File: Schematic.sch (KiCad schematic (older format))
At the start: 22 parts, among them J1 S2B-PH-K-S_LF__SN_, J2 Conn_01x04_Female, J3 Conn_02x05_Odd_Even, J4 Conn_01x05_Female, Q1 BSS138, Q2 BSS138, Q3 BSS138, U1 MDBT42Q, U2 AP7333-33SAG

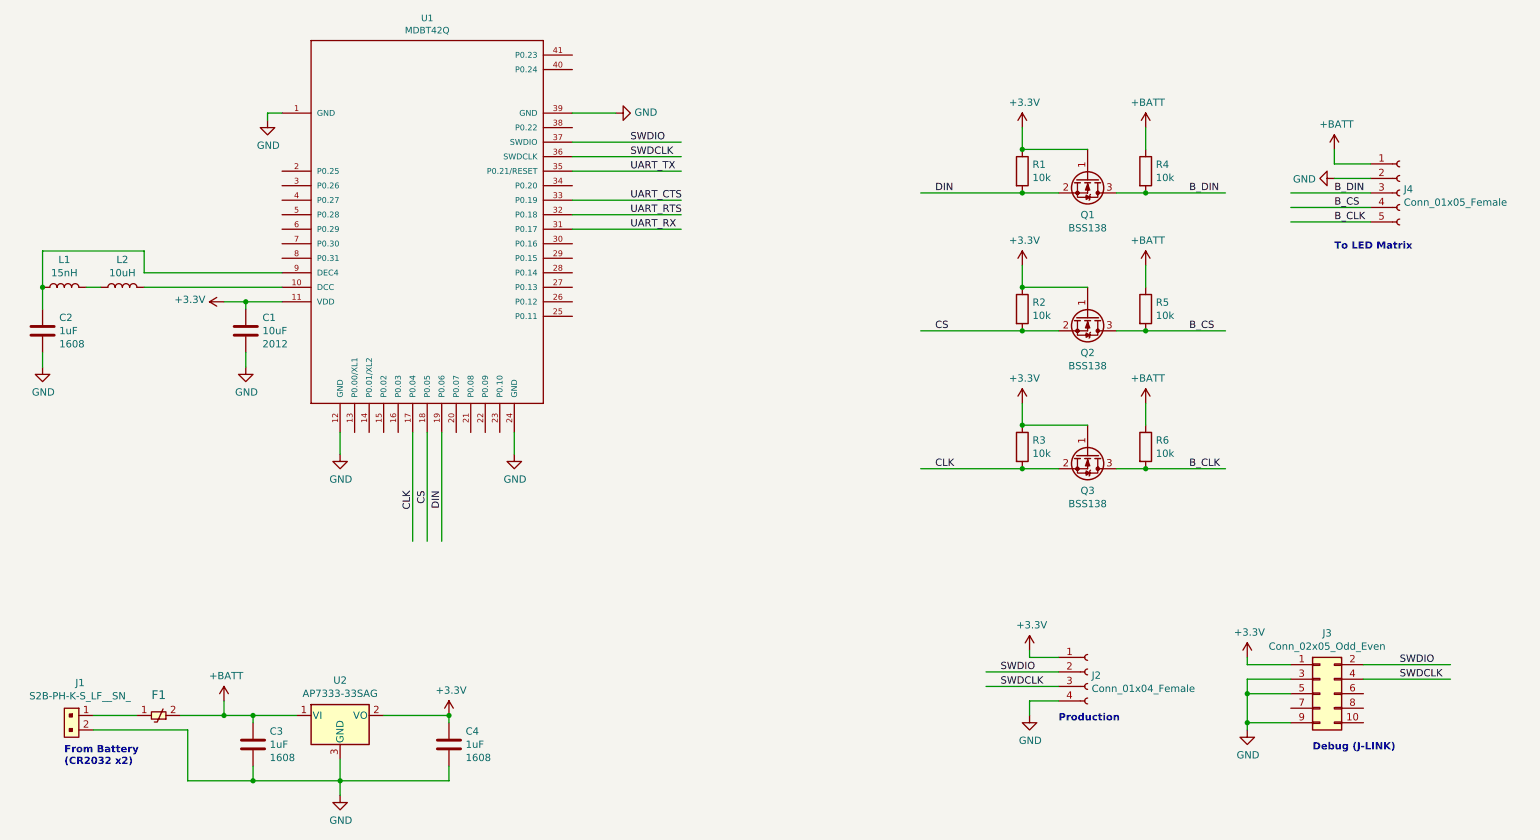
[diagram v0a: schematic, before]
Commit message: TP等を追加
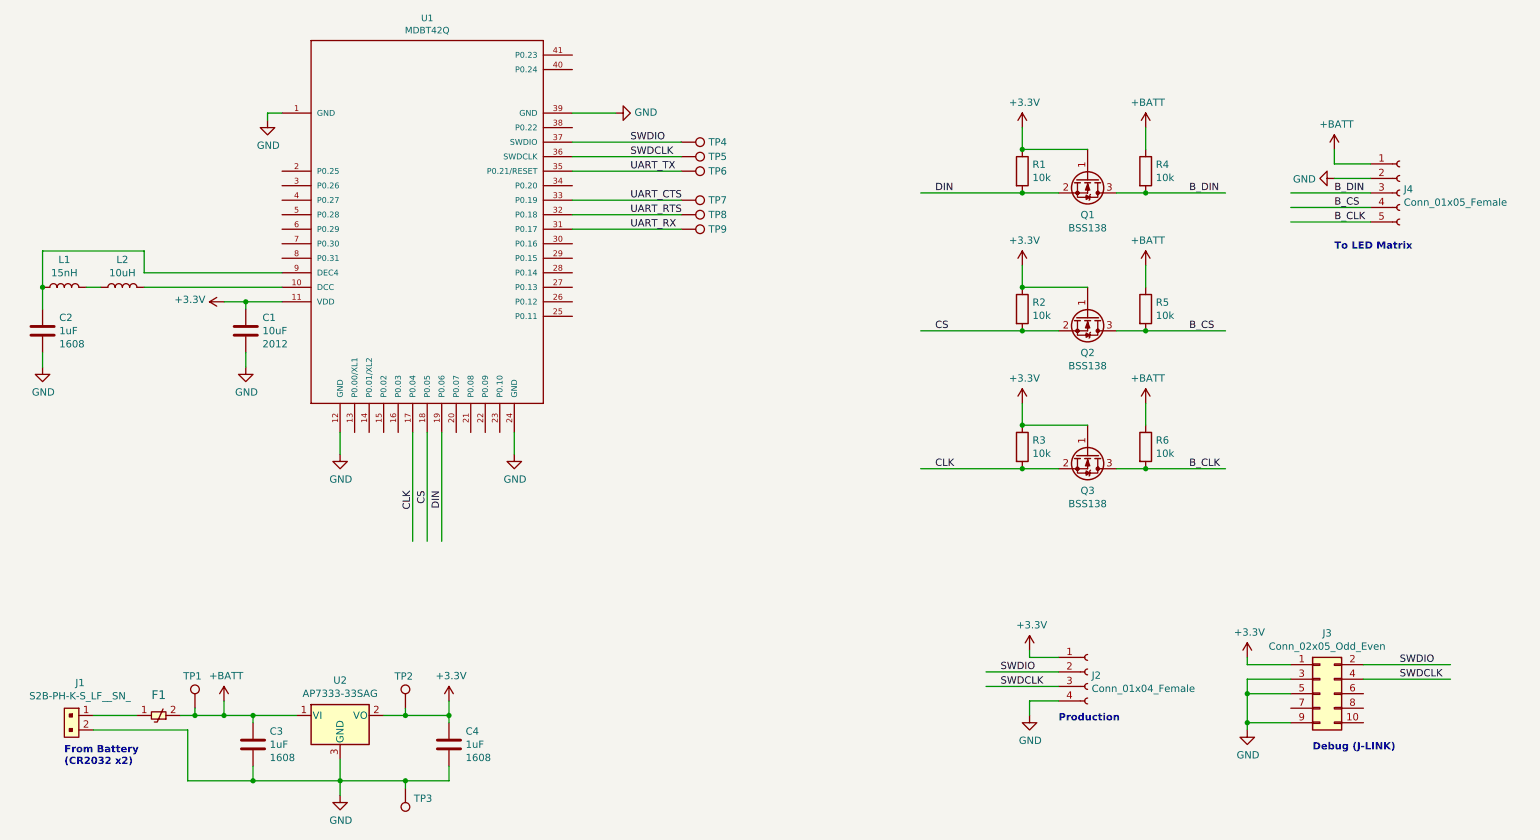
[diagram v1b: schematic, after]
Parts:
- added TP1, TP2, TP3, TP4, TP5, TP6, TP7, TP8, TP9: TestPoint, TestPoint:TestPoint_Pad_D1.5mm, symbol Connector:TestPoint
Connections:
- wire segments 86 -> 93
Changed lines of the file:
@@
 	4250 4200 4250 4050
-Wire Wire Line
-	5400 2050 4650 2050
 Wire Wire Line
 	5400 2150 4650 2150
@@
 Connection ~ 3050 6450
 Wire Wire Line
-	3050 6450 3800 6450
+	3050 6450 3500 6450
 Wire Wire Line
 	3800 6450 3800 6350
@@
 L power:+3.3V #PWR0118
 U 1 1 5D57A274
-P 3800 6000
-F 0 "#PWR0118" H 3800 5850 50  0001 C CNN
-F 1 "+3.3V" H 3815 6173 50  0000 C CNN
-F 2 "" H 3800 6000 50  0001 C CNN
-F 3 "" H 3800 6000 50  0001 C CNN
-	1    3800 6000
+P 3800 5900
+F 0 "#PWR0118" H 3800 5750 50  0001 C CNN
+F 1 "+3.3V" H 3815 6073 50  0000 C CNN
+F 2 "" H 3800 5900 50  0001 C CNN
+F 3 "" H 3800 5900 50  0001 C CNN
+	1    3800 5900
 	1    0    0    -1
 $EndComp
@@
 CLK
 Wire Wire Line
-	3350 6000 3800 6000
-Connection ~ 3800 6000
+	3350 6000 3500 6000
 $Comp
 L Regulator_Linear:APE8865NR-33-HF-3 U2
@@
 $EndComp
 Wire Wire Line
-	1950 6000 2250 6000
+	1950 6000 2050 6000
 Connection ~ 2250 6000
 Wire Wire Line
@@
 Wire Wire Line
 	1350 6100 2000 6100
+$Comp
+L Connector:TestPoint TP4
+U 1 1 5D697A64
+P 5400 2050
+F 0 "TP4" V 5400 2238 50  0000 L CNN
+F 1 "TestPoint" V 5445 2238 50  0001 L CNN
+F 2 "TestPoint:TestPoint_Pad_D1.5mm" H 5600 2050 50  0001 C CNN
+F 3 "~" H 5600 2050 50  0001 C CNN
+	1    5400 2050
+	0    1    1    0
+$EndComp
+Wire Wire Line
+	5400 2050 4650 2050
+$Comp
+L Connector:TestPoint TP5
+U 1 1 5D69C3EA
+P 5400 2150
+F 0 "TP5" V 5400 2338 50  0000 L CNN
+F 1 "TestPoint" V 5445 2338 50  0001 L CNN
+F 2 "TestPoint:TestPoint_Pad_D1.5mm" H 5600 2150 50  0001 C CNN
+F 3 "~" H 5600 2150 50  0001 C CNN
+	1    5400 2150
+	0    1    1    0
+$EndComp
+$Comp
+L Connector:TestPoint TP6
+U 1 1 5D69E66E
+P 5400 2250
+F 0 "TP6" V 5400 2438 50  0000 L CNN
+F 1 "TestPoint" V 5445 2438 50  0001 L CNN
+F 2 "TestPoint:TestPoint_Pad_D1.5mm" H 5600 2250 50  0001 C CNN
+F 3 "~" H 5600 2250 50  0001 C CNN
+	1    5400 2250
+	0    1    1    0
+$EndComp
+$Comp
+L Connector:TestPoint TP7
+U 1 1 5D6A08B9
+P 5400 2450
+F 0 "TP7" V 5400 2638 50  0000 L CNN
+F 1 "TestPoint" V 5445 2638 50  0001 L CNN
+F 2 "TestPoint:TestPoint_Pad_D1.5mm" H 5600 2450 50  0001 C CNN
+F 3 "~" H 5600 2450 50  0001 C CNN
+	1    5400 2450
+	0    1    1    0
+$EndComp
+$Comp
+L Connector:TestPoint TP8
+U 1 1 5D6A29FA
+P 5400 2550
+F 0 "TP8" V 5400 2738 50  0000 L CNN
+F 1 "TestPoint" V 5445 2738 50  0001 L CNN
+F 2 "TestPoint:TestPoint_Pad_D1.5mm" H 5600 2550 50  0001 C CNN
+F 3 "~" H 5600 2550 50  0001 C CNN
+	1    5400 2550
+	0    1    1    0
+$EndComp
+$Comp
+L Connector:TestPoint TP9
+U 1 1 5D6A4C7E
+P 5400 2650
+F 0 "TP9" V 5400 2838 50  0000 L CNN
+F 1 "TestPoint" V 5445 2838 50  0001 L CNN
+F 2 "TestPoint:TestPoint_Pad_D1.5mm" H 5600 2650 50  0001 C CNN
+F 3 "~" H 5600 2650 50  0001 C CNN
+	1    5400 2650
+	0    1    1    0
+$EndComp
+$Comp
+L Connector:TestPoint TP2
+U 1 1 5D6A7498
+P 3500 5950
+F 0 "TP2" H 3425 6170 50  0000 L CNN
+F 1 "TestPoint" V 3545 6138 50  0001 L CNN
+F 2 "TestPoint:TestPoint_Pad_D1.5mm" H 3700 5950 50  0001 C CNN
+F 3 "~" H 3700 5950 50  0001 C CNN
+	1    3500 5950
+	1    0    0    -1
+$EndComp
+$Comp
+L Connector:TestPoint TP1
+U 1 1 5D6AA1A3
+P 2050 5950
+F 0 "TP1" H 1969 6171 50  0000 L CNN
+F 1 "TestPoint" V 2095 6138 50  0001 L CNN
+F 2 "TestPoint:TestPoint_Pad_D1.5mm" H 2250 5950 50  0001 C CNN
+F 3 "~" H 2250 5950 50  0001 C CNN
+	1    2050 5950
+	1    0    0    -1
+$EndComp
+$Comp
+L Connector:TestPoint TP3
+U 1 1 5D6AD4E4
+P 3500 6500
+F 0 "TP3" H 3442 6572 50  0000 R CNN
+F 1 "TestPoint" V 3545 6688 50  0001 L CNN
+F 2 "TestPoint:TestPoint_Pad_D1.5mm" H 3700 6500 50  0001 C CNN
+F 3 "~" H 3700 6500 50  0001 C CNN
+	1    3500 6500
+	-1   0    0    1
+$EndComp
+Wire Wire Line
+	2050 5950 2050 6000
+Connection ~ 2050 6000
+Wire Wire Line
+	2050 6000 2250 6000
+Wire Wire Line
+	3500 5950 3500 6000
+Connection ~ 3500 6000
+Wire Wire Line
+	3500 6000 3800 6000
+Wire Wire Line
+	3800 6000 3800 5900
+Connection ~ 3800 6000
+Wire Wire Line
+	3500 6500 3500 6450
+Connection ~ 3500 6450
+Wire Wire Line
+	3500 6450 3800 6450
 $EndSCHEMATC
